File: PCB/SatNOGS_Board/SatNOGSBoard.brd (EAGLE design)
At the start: 59.4 x 68.6 mm, 17 parts, among them J1 2, J2 3, J3 4

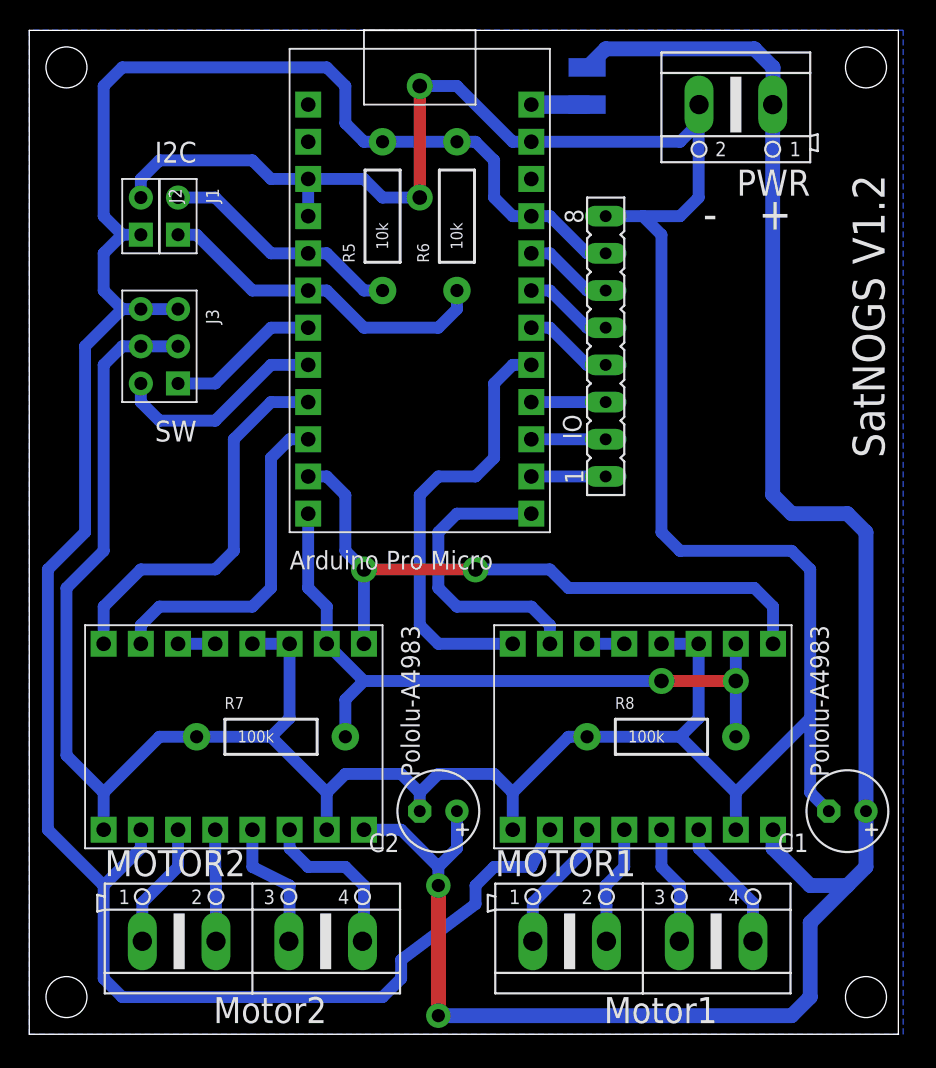
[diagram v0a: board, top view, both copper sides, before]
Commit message: schematic update, raw routing prototype
this adds the AtMega168 and neccesary components. Layout is just a raw
sketch, someone should finish that.
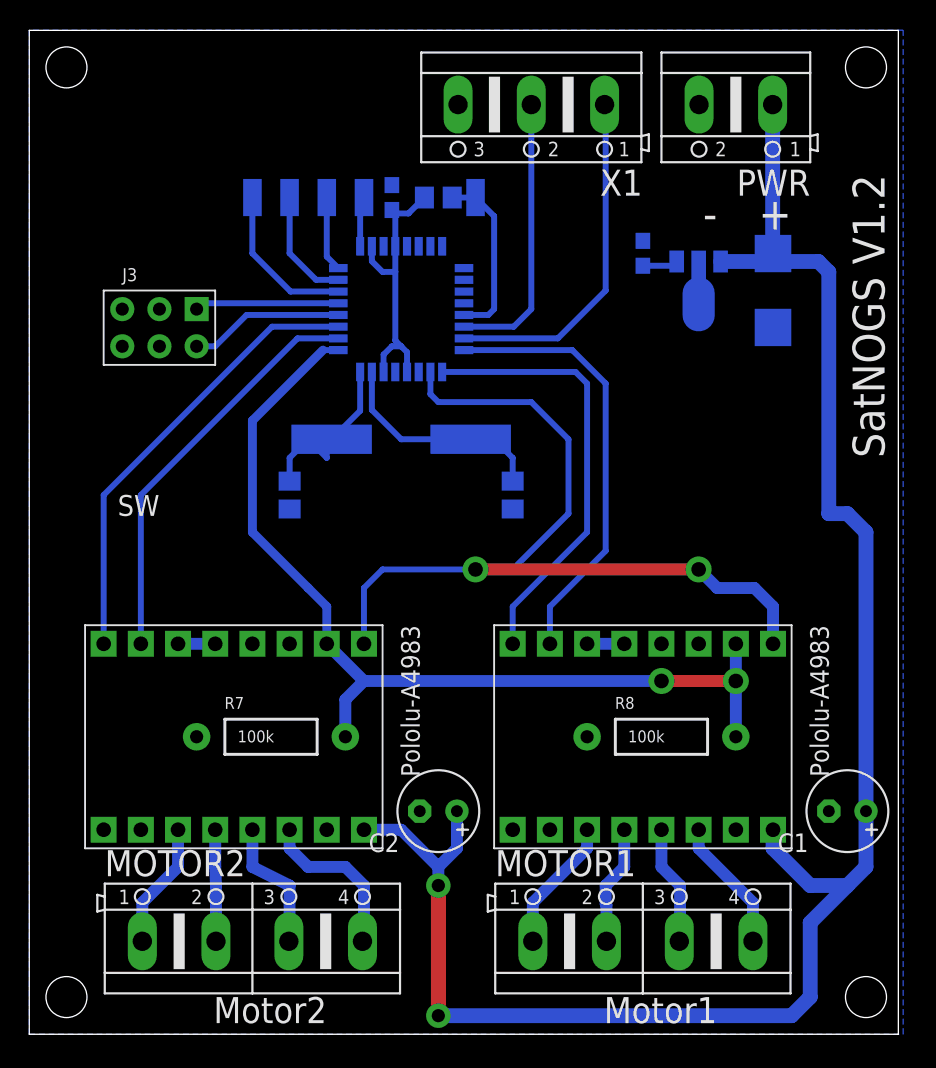
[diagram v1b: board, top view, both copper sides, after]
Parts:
- removed IO: 1, con-lsta:FE08
- removed J1: 2, Connector:2P-2.54-65/35MIL
- removed J2: 3, Connector:2P-2.54-65/35MIL
- removed R5, R6: 10k, SparkFun-Resistors:AXIAL-0.4
- removed SJ1: SJ1, jumper:SJW
- removed UC: ARDUINO_PRO_MICROARDUINO_BOARD, Arduino_Pro_Micro:ARDUINO_MICRO_PRO
- added C3, C4: 18p, rcl:C0805
- added C5, C6: 100n, rcl:C0603
- added C7: (no value), rcl:C/6032-28R
- added IC1: MEGA8-AI, atmel:TQFP32-08
- added IC2: 78L05F, linear:SOT89
- added PAD1, PAD2, PAD3, PAD4, PAD5: (no value), wirepad:SMD1,27-2,54
- added Q1: 16MHz, crystal:CSM-7X-DU
- added R1: 10k, rcl:R0805
- added X1: (no value), con-ptr500:AK500/3
- moved J3 1.27 mm to (8.89, 48.3), turned to 270 degrees
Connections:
- removed net IO1: IO.6, UC.20
- removed net IO2: IO.5, UC.19
- removed net IO3: IO.4, UC.18
- removed net IO4: IO.3, UC.16
- removed net IO5: IO.2, UC.15
- removed net IO6: IO.1, UC.14
- removed net SCL: J1.1, R6.P$1, UC.6
- removed net SDA: J1.2, R5.P$1, UC.5
- removed net VCC: DRIVER1.10, DRIVER2.10, IO.7, J2.1, J3.3, J3.4, R5.P$2, R6.P$2, UC.21
- new net +5V: C5.1, C6.1, DRIVER1.10, DRIVER2.10, IC1.18, IC1.20, IC1.4, IC1.6, IC2.1, J3.3, J3.4, R1.2
- new net N$10: IC1.16, PAD2.1
- new net N$11: IC1.17, PAD1.1
- new net N$4: C3.2, IC1.7, Q1.2
- new net N$5: IC1.29, PAD5.1, R1.1
- new net N$6: C4.2, IC1.8, Q1.1
- new net N$7: IC1.30, X1.2
- new net N$8: IC1.14, PAD4.1
- new net N$9: IC1.15, PAD3.1
- net DIR-1: now also IC1.1; no longer UC.17
- net DIR-2: now also IC1.11; no longer UC.9
- net GND: now also C3.1, C4.1, C5.2, C6.2, C7.-, IC1.21, IC1.3, IC1.5, IC2.2, IC2.2@1, X1.3; no longer IO.8, J2.2, UC.23, UC.3, UC.4
- net MS1: now also IC1.9; no longer UC.12
- net M_EN: now also IC1.2; no longer UC.11
- net N$3: now also IC1.31, X1.1; no longer SJ1.1, UC.24
- net STEP-1: now also IC1.32; no longer UC.13
- net STEP-2: now also IC1.10; no longer UC.10
- net SW1: now also IC1.13; no longer UC.7
- net SW2: now also IC1.12; no longer UC.8
- net VMOTOR: now also C7.+, IC2.3; no longer SJ1.2
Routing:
- net GND: track 242.8 -> 0.00 mm, vias 2 -> 0
- net VCC: track 156.7 -> 0.00 mm
- net SCL: track 23.5 -> 0.00 mm
- net +5V: track 0.00 -> 21.9 mm
- net N$3: track 3.81 -> 23.8 mm
- net N$7: track 0.00 -> 19.1 mm
- net SDA: track 16.6 -> 0.00 mm
- net M_EN: track 45.3 -> 61.1 mm
- net MS1: track 49.1 -> 64.9 mm
- net N$4: track 0.00 -> 15.2 mm
- net N$6: track 0.00 -> 12.0 mm
- net N$5: track 0.00 -> 12.0 mm
- net N$8: track 0.00 -> 10.8 mm
- net STEP-1: track 20.6 -> 30.0 mm
- net VMOTOR: track 137.7 -> 128.5 mm
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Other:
- board text removed: "I2C"

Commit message: board routing
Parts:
- removed J3: 4, Connector:2X3P-2.54-65/35MIL
- removed PAD1, PAD2, PAD3, PAD4, PAD5: (no value), wirepad:SMD1,27-2,54
- removed X1: (no value), con-ptr500:AK500/3
- added C10, C11, C12, C13, C14, C15, C16, C17, C18, C19, C8: 680n, rcl:C1206
- added C9: 100n, rcl:C0805
- added D1, D2: BAV99, diode:SOT23
- added FB1: 10R@100MHz, SparkFun-Resistors:0805
- added JP1, JP2, JP3: (no value), pinhead:1X03
- added MISO, MOSI, RES, SCK: (no value), wirepad:SMD1,27-2,54
- added R2: 1k, SparkFun-Resistors:0805
- added R3: 475R, SparkFun-Resistors:0805
- added R4, R5: (no value), SparkFun-Resistors:0603-RES
- added R6, R9: 0R, SparkFun-Resistors:1206
- C3, C4: device rcl:C0805 -> rcl:C1206
- C5: device rcl:C0603 -> rcl:C0805
- R1: value 10k -> 4k7
- R7, R8: device SparkFun-Resistors:AXIAL-0.4 -> SparkFun-Resistors:0805
- moved C1 53.7 mm to (2.54, 21.6), flipped to the bottom, turned to 270 degrees
- moved C7 45.9 mm to (5.08, 54.6), flipped to the top
- moved PWR 36.9 mm to (11.4, 64.8), flipped to the bottom
- moved IC2 34.5 mm to (11.4, 54.6), flipped to the top
- moved DRIVER2 30.1 mm to (43.8, 24.1), flipped to the bottom
- moved MOTOR2 28.6 mm to (43.8, 7.62), flipped to the bottom
- moved C5 26.7 mm to (15.2, 54.6), flipped to the top, turned to 270 degrees
- moved DRIVER1 26.3 mm to (15.9, 24.1), flipped to the bottom
- moved MOTOR1 26.1 mm to (15.9, 7.62), flipped to the bottom
- moved C4 20.2 mm to (37.1, 42.7), flipped to the top, turned to 180 degrees
- moved C6 16.2 mm to (31.8, 42.5), flipped to the top, turned to 180 degrees
- moved R7 13.4 mm to (10.8, 32.4), turned to 180 degrees
- moved R8 9.38 mm to (38.7, 28.6), turned to 180 degrees
- moved Q1 7.96 mm to (32.7, 37.5), flipped to the top
- moved C2 6.63 mm to (29.8, 21.6), flipped to the bottom, turned to 270 degrees
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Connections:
- net N$4 renamed XTAL1
- net N$6 renamed XTAL2
- removed net VMOTOR: C1.+, C2.+, C7.+, DRIVER1.16, DRIVER2.16, IC2.3, PWR.1
- new net +12V: C1.+, C12.1, C13.1, C14.1, C15.1, C16.1, C17.1, C18.1, C19.1, C2.+, C7.+, C9.1, DRIVER1.16, DRIVER2.16, IC2.3, PWR.1
- new net +5VM: C10.1, DRIVER1.10, DRIVER2.10, FB1.2
- new net N$12: IC1.12, R4.1
- new net N$13: DRIVER2.3, DRIVER2.4, R6.2, R8.1
- new net N$14: JP2.2, JP3.2, R9.1
- new net N$4: D2.3, JP1.3, R3.2
- new net N$6: IC1.30, R2.1
- net +5V: now also C11.1, C8.1, D1.2, D2.2, FB1.1, R9.2; no longer DRIVER1.10, DRIVER2.10, IC1.20, J3.3, J3.4
- net GND: now also C10.2, C11.2, C12.2, C13.2, C14.2, C15.2, C16.2, C17.2, C18.2, C19.2, C8.2, C9.2, D1.1, D2.1, JP1.2, JP2.3, JP3.3, R6.1, R7.1; no longer DRIVER2.3, DRIVER2.4, J3.2, J3.5, R7.P$1, R8.P$1, X1.3
- net MS1: now also R7.2, R8.2; no longer R7.P$2, R8.P$2
- net N$10: now also MISO.1; no longer PAD2.1
- net N$11: now also SCK.1; no longer PAD1.1
- net N$3: now also D1.3, JP1.1, R2.2; no longer IC1.31, X1.1
- net N$5: now also RES.1; no longer PAD5.1
- net N$7: now also IC1.31, R3.1; no longer IC1.30, X1.2
- net N$8: now also IC1.13, R5.1; no longer IC1.14, PAD4.1
- net N$9: now also MOSI.1; no longer PAD3.1
- net SW1: now also JP2.1, R5.2; no longer IC1.13, J3.1
- net SW2: now also JP3.1, R4.2; no longer IC1.12, J3.6
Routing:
- net GND: track 0.00 -> 278.9 mm
- net +5VM: track 0.00 -> 150.3 mm
- net VMOTOR: track 128.5 -> 0.00 mm, vias 2 -> 0
- net +12V: track 0.00 -> 55.2 mm
- net +5V: track 21.9 -> 71.2 mm
- net N$14: track 0.00 -> 26.2 mm
- net N$3: track 23.8 -> 7.04 mm
- net N$6: track 0.00 -> 9.72 mm
- net N$13: track 0.00 -> 8.50 mm
- net N$4: track 0.00 -> 7.04 mm
- net MS1: track 64.9 -> 71.9 mm, vias 2 -> 0
- net N$12: track 0.00 -> 6.96 mm
- net DIR-1: track 30.1 -> 23.5 mm
- net STEP-1: track 30.0 -> 23.7 mm
- net N$5: track 12.0 -> 17.8 mm
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- added copper zone on layer 1, net +12V
- added copper zone on layer 1, net GND
- removed copper zone on layer 16, net GND
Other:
- board size 59.4 x 68.6 mm -> 59.4 x 64.8 mm
- board text added: "4714 YC"
- board text added: "SatNOGS Rotor Control"
- board text removed: "+"
- board text removed: "-"
- board text removed: "Motor1"
- board text removed: "Motor2"
- board text removed: "SW"
- board text removed: "SatNOGS V1.2"
